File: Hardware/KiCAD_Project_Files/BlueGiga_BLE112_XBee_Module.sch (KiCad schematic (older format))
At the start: 9 parts, among them P1 XBEE HEADER, P2 DEBUG, U1 BLE112-A

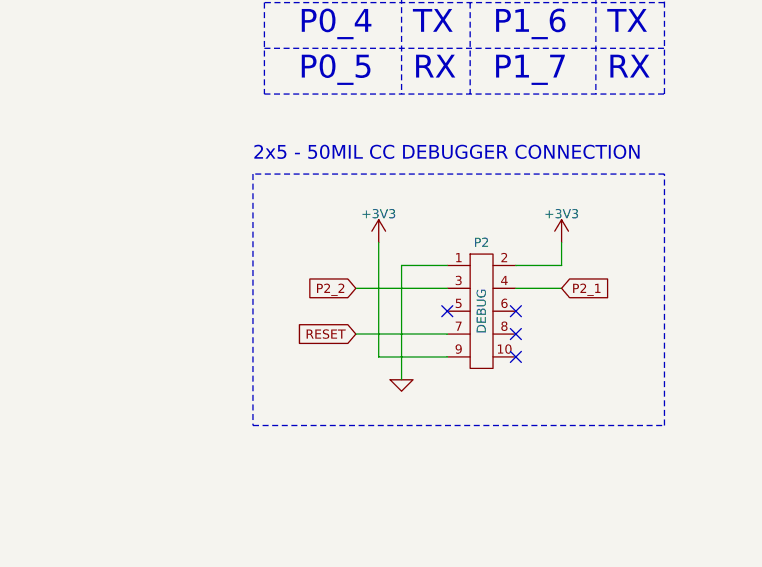
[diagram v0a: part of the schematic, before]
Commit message: Corrected debug header connections where pin 9 was connected to 3.3V.
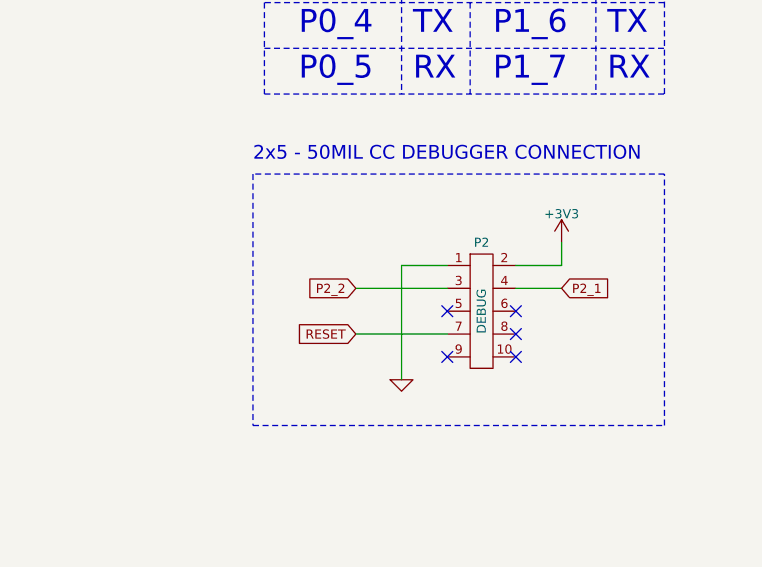
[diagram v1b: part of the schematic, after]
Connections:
- net +3V3: no longer P2.9
- no-connect marks 32 -> 33
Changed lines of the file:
@@
 	9150 3950 9350 3950
-Wire Wire Line
-	9350 4350 9050 4350
-Wire Wire Line
-	9050 4350 9050 3850
 Wire Wire Line
 	9350 4050 8950 4050
@@
 $EndComp
 $Comp
-L +3V3 #PWR014
-U 1 1 553BA15B
-P 9050 3850
-F 0 "#PWR014" H 9050 3700 50  0001 C CNN
-F 1 "+3V3" H 9050 3975 40  0000 C CNN
-F 2 "" H 9050 3850 60  0000 C CNN
-F 3 "" H 9050 3850 60  0000 C CNN
-	1    9050 3850
-	1    0    0    -1
-$EndComp
-$Comp
 L +3V3 #PWR015
 U 1 1 553BA2DC
@@
 Wire Wire Line
 	3075 5250 4175 5250
+NoConn ~ 9350 4350
 $EndSCHEMATC
